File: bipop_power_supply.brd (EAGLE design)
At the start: 82.5 x 70.8 mm, 23 parts, among them IC1 LM1117MP-3.3, IC2 LM1117MP-5.0, X2 MSTBA6

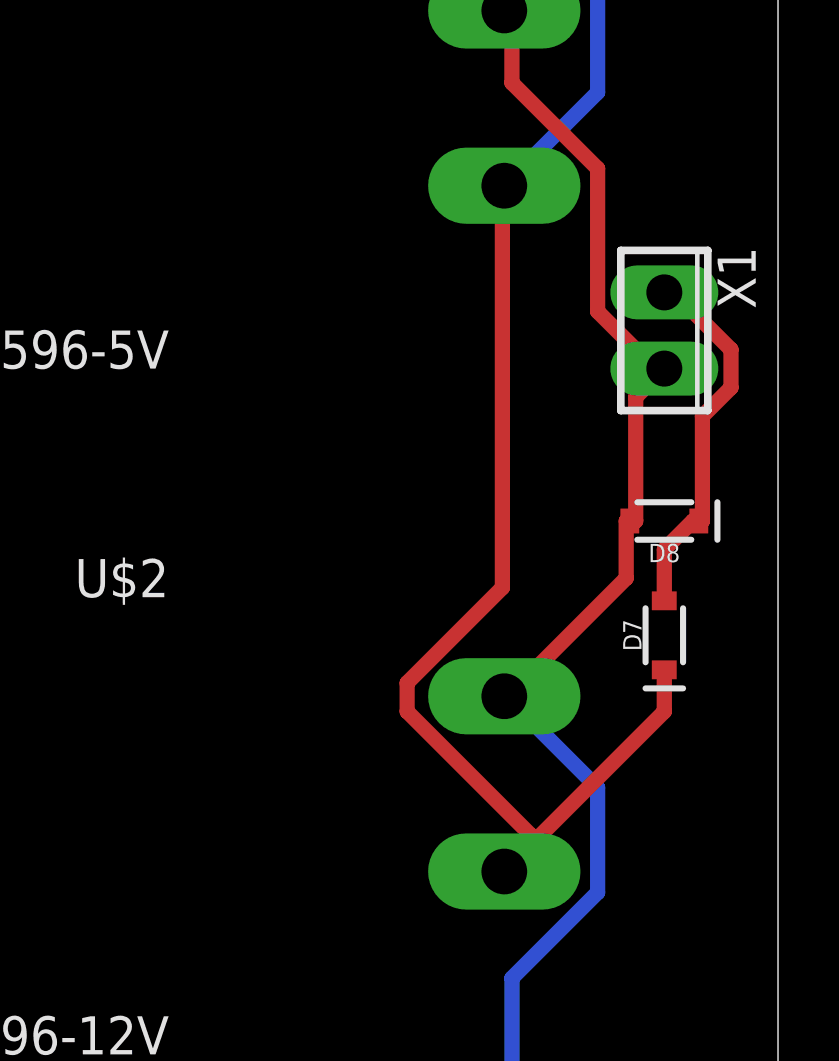
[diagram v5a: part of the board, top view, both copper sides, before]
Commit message: Circuit converted to single-periscope operation mode. Duplicate components removed.
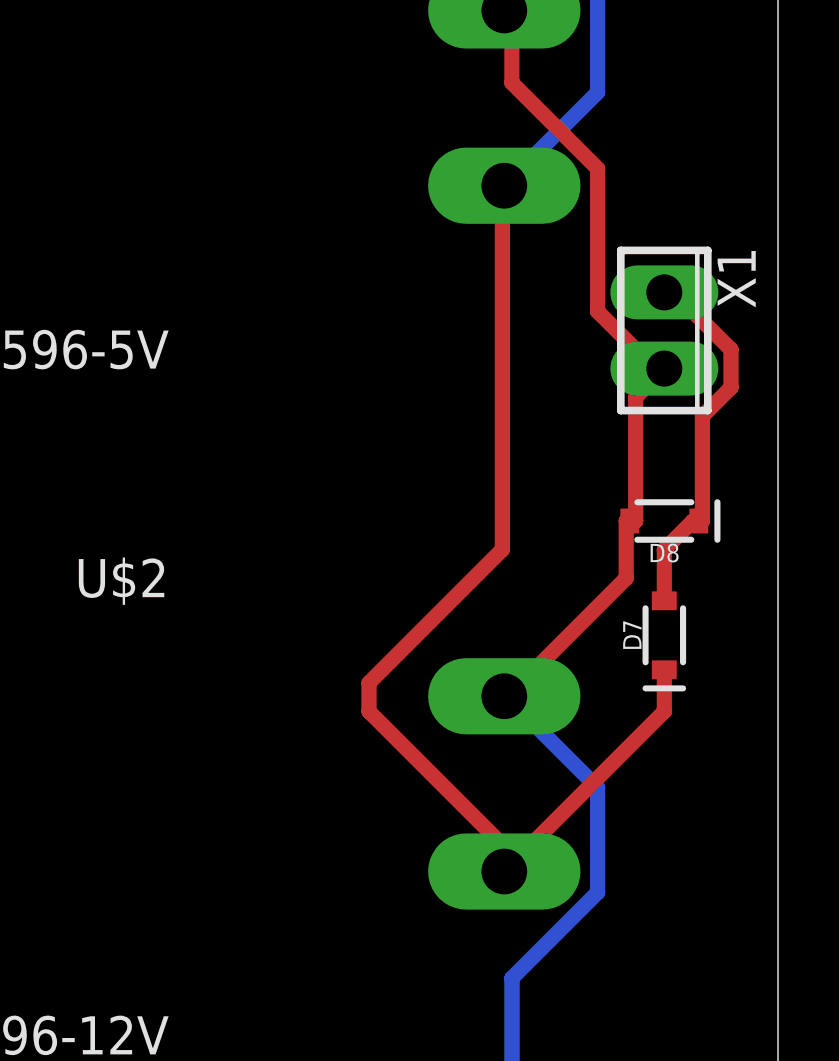
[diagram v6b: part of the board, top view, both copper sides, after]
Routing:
- net N$22: track 60.7 -> 62.4 mm
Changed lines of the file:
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@@
 <wire x1="82.55" y1="26.67" x2="82.55" y2="28.06" width="0.508" layer="1"/>
 <wire x1="77.216" y1="21.336" x2="82.55" y2="26.67" width="0.508" layer="1"/>
-<wire x1="77.1525" y1="30.7975" x2="77.1525" y2="44.1325" width="0.508" layer="1"/>
-<wire x1="73.9775" y1="27.6225" x2="77.1525" y2="30.7975" width="0.508" layer="1"/>
-<wire x1="73.9775" y1="26.67" x2="73.9775" y2="27.6225" width="0.508" layer="1"/>
-<wire x1="78.105" y1="22.5425" x2="73.9775" y2="26.67" width="0.508" layer="1"/>
+<wire x1="77.1525" y1="32.0675" x2="77.1525" y2="44.1325" width="0.508" layer="1"/>
+<wire x1="72.7075" y1="27.6225" x2="77.1525" y2="32.0675" width="0.508" layer="1"/>
+<wire x1="72.7075" y1="26.67" x2="72.7075" y2="27.6225" width="0.508" layer="1"/>
+<wire x1="78.105" y1="21.2725" x2="72.7075" y2="26.67" width="0.508" layer="1"/>
 <wire x1="77.1525" y1="44.1325" x2="77.216" y2="44.196" width="0.508" layer="1"/>
-<wire x1="78.105" y1="22.5425" x2="77.216" y2="21.336" width="0.508" layer="1"/>
+<wire x1="78.105" y1="21.2725" x2="77.216" y2="21.336" width="0.508" layer="1"/>
 <wire x1="77.47" y1="53.6575" x2="77.47" y2="66.9925" width="0.508" layer="16"/>
 <wire x1="80.3275" y1="50.8" x2="77.47" y2="53.6575" width="0.508" layer="16"/>

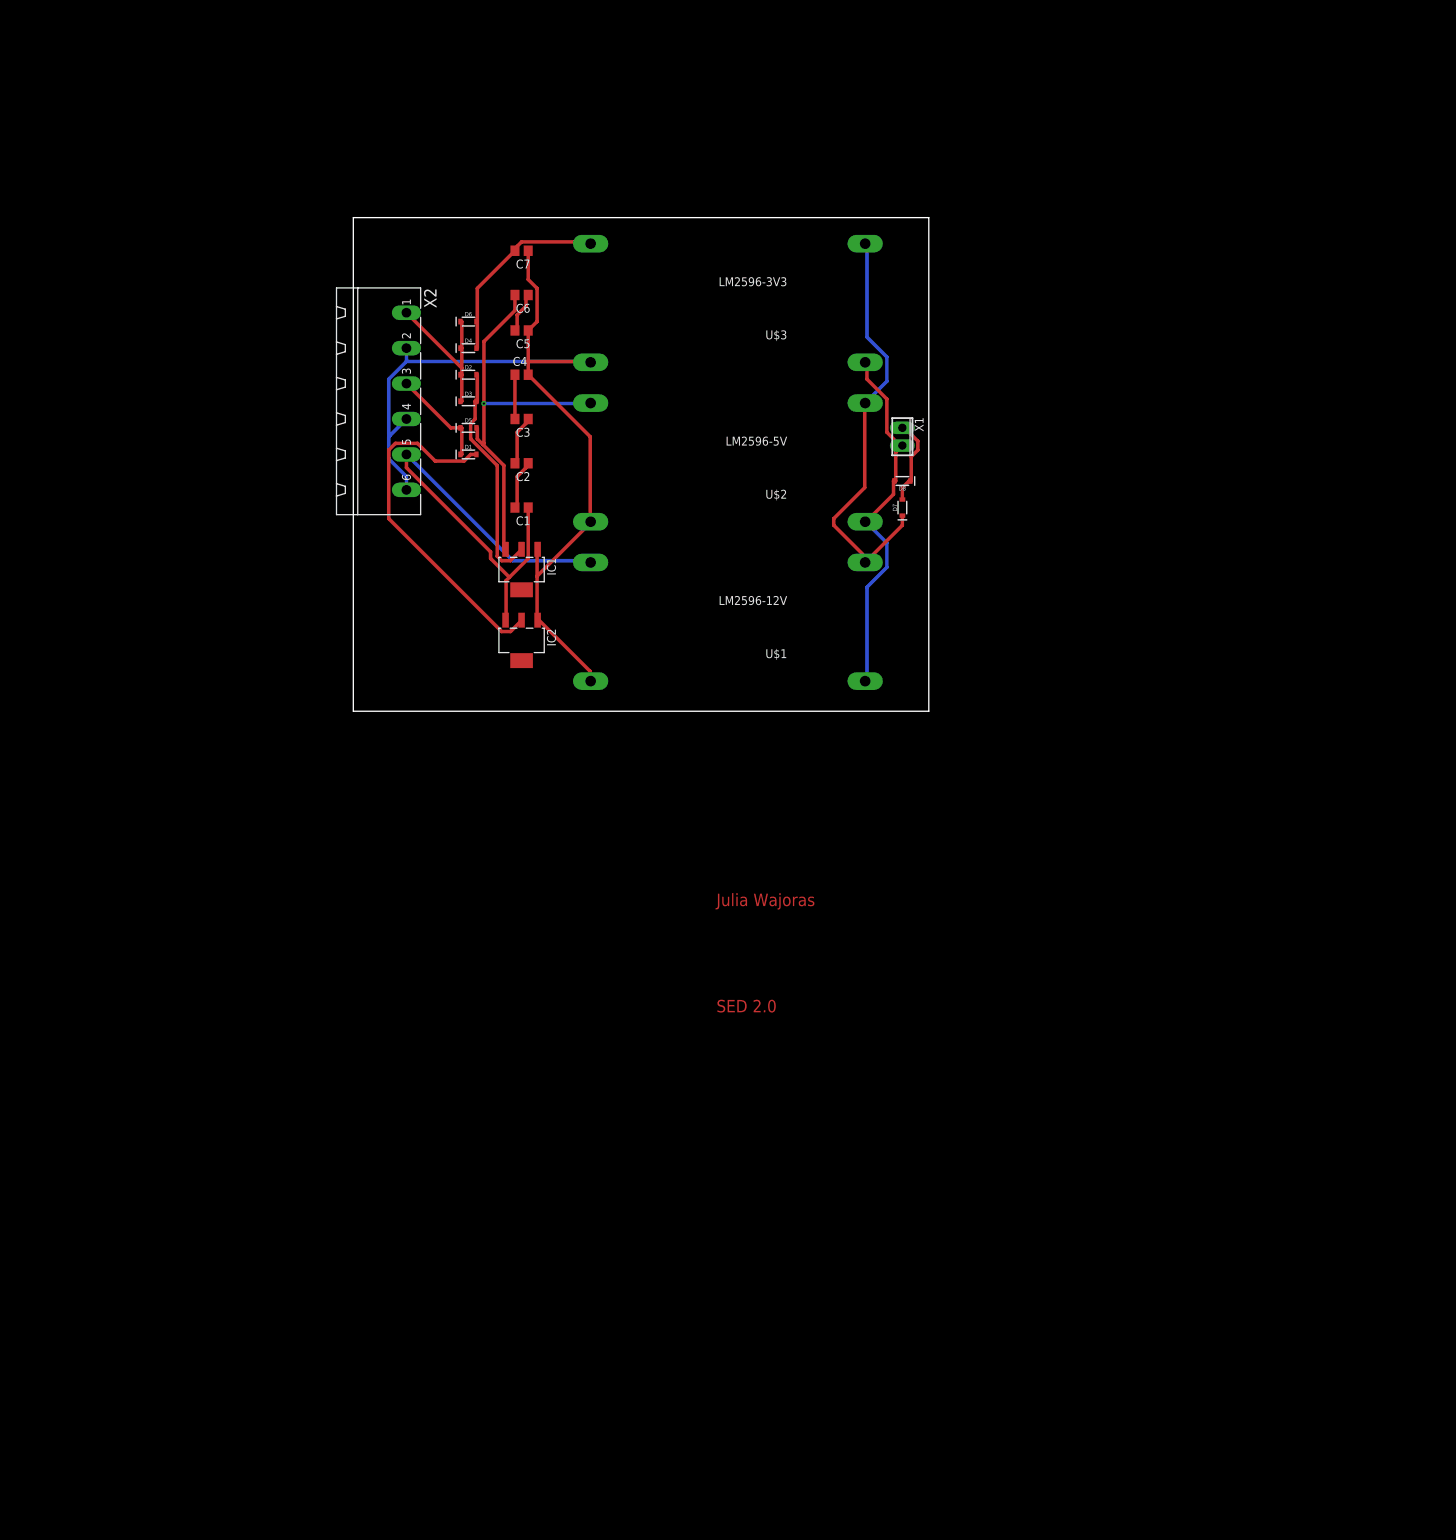
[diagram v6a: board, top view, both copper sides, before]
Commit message: added current sensors to power supply, NO ADC yet
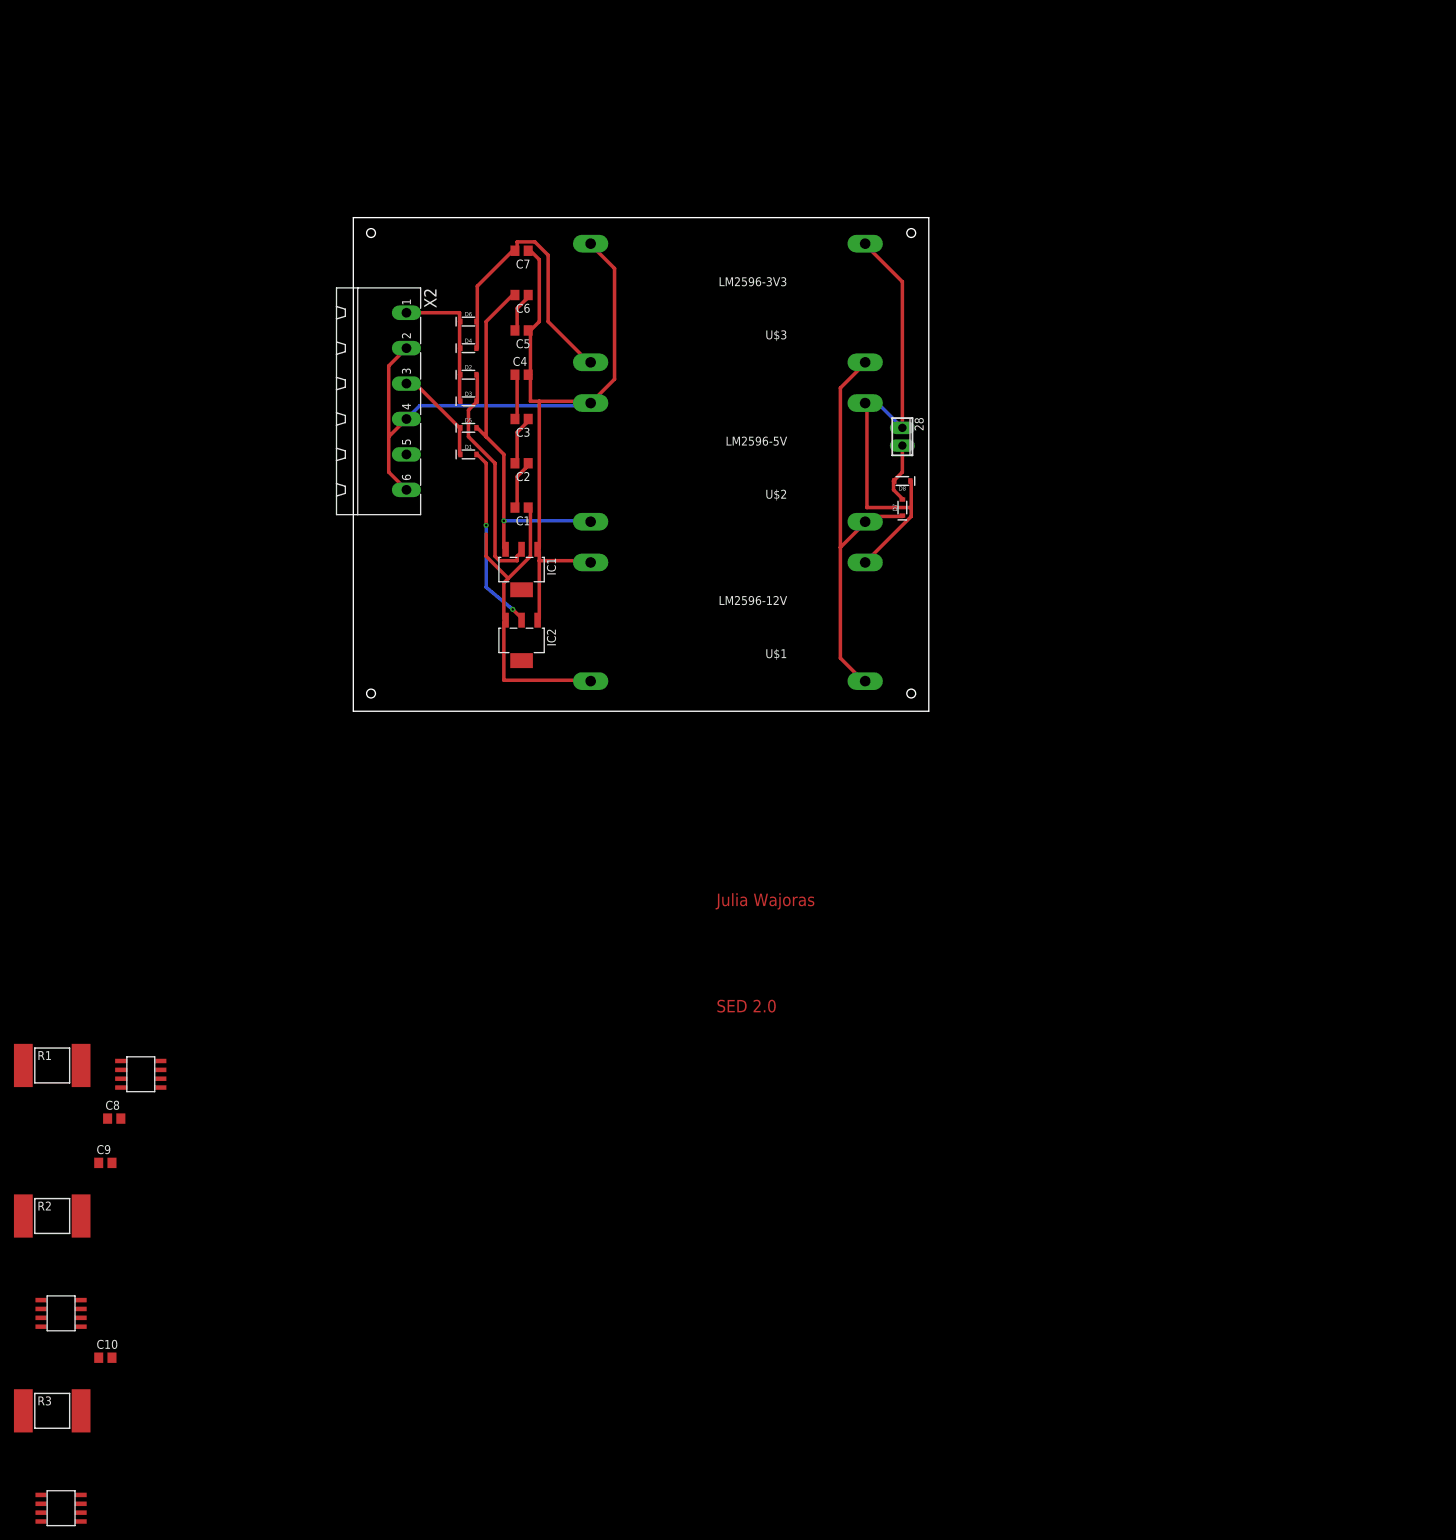
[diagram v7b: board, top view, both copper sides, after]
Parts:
- added C10, C8, C9: 0.1uF, rcl:C0805
- added R1, R2, R3: 4.7k, resistor-shunt:BVS
- added U$5, U$6, U$7: ACS711, lustro_pcb:ACS711
- renumbered X1 to 28
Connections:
- removed net C12+: C1.1, IC2.3, U$1.V_OUT+, X2.5
- removed net N$22: D7.C, U$1.V_IN+, U$2.V_IN+, U$3.V_IN+
- removed net N$7: C7.2, D4.A, D6.A, U$3.V_OUT+
- new net 12_IN: C1.1, IC2.3, U$1.V_OUT+, U$5.IP+_1, U$5.IP+_2
- new net 12_OUT: U$5.IP-_1, U$5.IP-_2, X2.5
- new net 3_OUT: C7.2, D4.A, D6.A, U$7.IP-_1, U$7.IP-_2
- new net 5_IN: C6.2, U$2.V_OUT+, U$6.IP+_1, U$6.IP+_2
- new net 5_OUT: D5.A, IC1.3, U$6.IP-_1, U$6.IP-_2
- new net N$12: 28.2, D7.A, D8.A
- new net N$13: R2.2, U$6.FAULT
- new net N$14: U$3.V_OUT+
- new net VCC_3V3: C10.1, C8.1, C9.1, D7.C, R1.1, R2.1, R3.1, U$1.V_IN+, U$2.V_IN+, U$3.V_IN+, U$5.VCC, U$6.VCC, U$7.IP+_1, U$7.IP+_2, U$7.VCC
- new net VIOUT_12: U$5.VIOUT
- new net VIOUT_3: U$7.VIOUT
- new net VIOUT_5: U$6.VIOUT
- net GND: now also C10.2, C8.2, C9.2, U$5.GND, U$6.GND, U$7.GND
- net N$1: now also R1.2, U$5.FAULT; no longer 28.2, D8.A, U$1.V_IN-, U$2.V_IN-, U$3.V_IN-
- net N$10: now also U$1.V_IN-, U$2.V_IN-, U$3.V_IN-; no longer D7.A
- net N$4: now also R3.2, U$7.FAULT; no longer C6.2, D5.A, IC1.3, U$2.V_OUT+
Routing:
- net C12+: track 74.1 -> 0.00 mm
- net N$22: track 62.4 -> 0.00 mm
- net VCC_3V3: track 0.00 -> 60.0 mm
- net N$10: track 12.5 -> 71.4 mm
- net N$4: track 57.9 -> 0.00 mm, vias 1 -> 0
- net N$1: track 53.2 -> 0.00 mm
- net 5_OUT: track 0.00 -> 53.2 mm, vias 0 -> 1
- net 12_IN: track 0.00 -> 46.6 mm
- net 3_OUT: track 0.00 -> 41.1 mm
- net N$7: track 28.4 -> 0.00 mm
- net N$3: track 50.7 -> 26.7 mm, vias 0 -> 2
- net GND: track 138.2 -> 150.5 mm
- net N$12: track 0.00 -> 8.91 mm
- net N$11: track 23.4 -> 20.8 mm
- net N$5: track 32.8 -> 33.7 mm
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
